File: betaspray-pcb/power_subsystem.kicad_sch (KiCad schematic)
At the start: 1 part, among them U2 LM3940IT-3.3

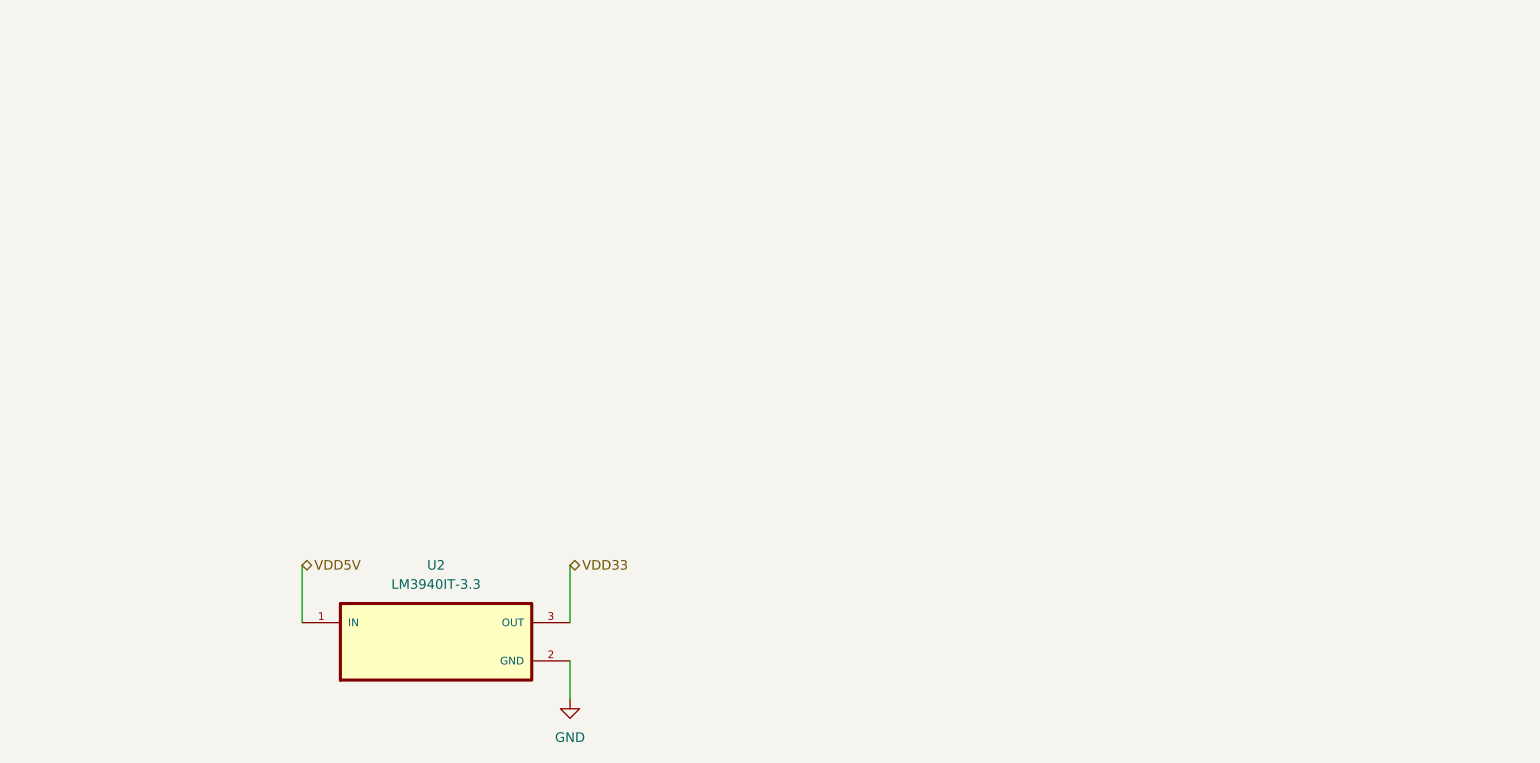
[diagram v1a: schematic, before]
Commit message: Add USB-C, connection, power decoupling
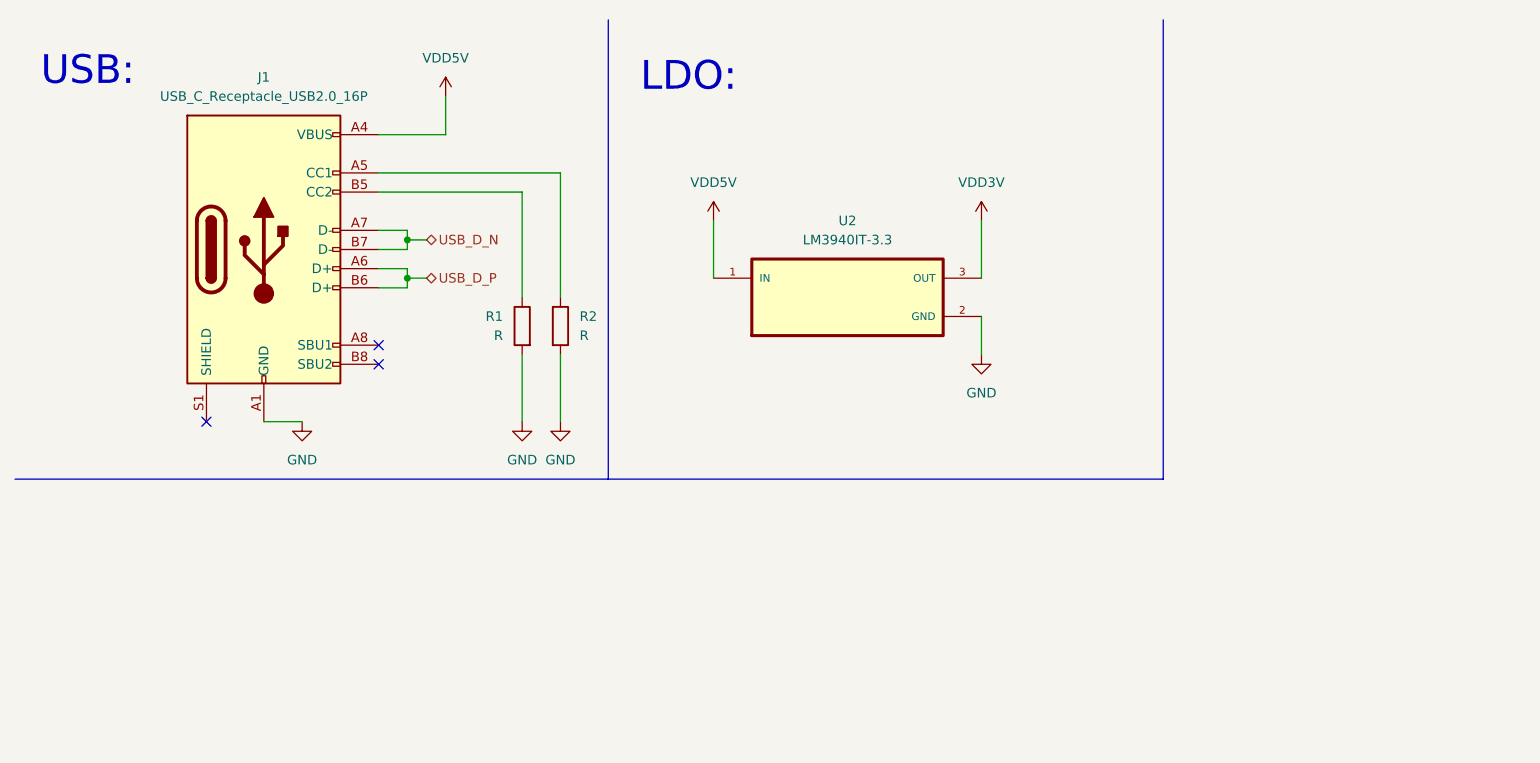
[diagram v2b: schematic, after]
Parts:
- added J1: USB_C_Receptacle_USB2.0_16P, Connector_USB:USB_C_Receptacle_G-Switch_GT-USB-7010ASV, symbol betaspray_Connector:USB_C_Receptacle_USB2.0_16P
- added R1, R2: R, symbol betaspray_LDO:R
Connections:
- net GND: now also J1.A1 (GND), J1.A12 (GND), J1.B1 (GND), J1.B12 (GND), R1.2, R2.2
- net VDD5V: now also J1.A4 (VBUS), J1.A9 (VBUS), J1.B4 (VBUS), J1.B9 (VBUS)
- net VDD33 renamed VDD3V
- new net: J1.B5 (CC2), R1.1
- new net: J1.A5 (CC1), R2.1
- new net USB_D_N: J1.A7 (D-), J1.B7 (D-)
- new net USB_D_P: J1.A6 (D+), J1.B6 (D+)
- no-connect marks 0 -> 3
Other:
- note added: "LDO:"
- note added: "USB:"
- moved on the sheet: U2

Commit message: status led ???
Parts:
- added C4: 0.47 uF, symbol betaspray_LDO:C
- added C5: 33 uF, symbol Device:C
- added D1: LED, LED_SMD:LED_0805_2012Metric, symbol betaspray_LDO:LED
- added R3: 300, symbol betaspray_LDO:R
- R1, R2: value R -> 5.1k
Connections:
- net GND: now also C4.2, C5.2, R3.2
- net VDD3V: now also C5.1, D1.2 (A)
- net VDD5V: now also C4.1
- new net: D1.1 (K), R3.1
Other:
- note added: "These are the recommended input/output capacitance, per TI's datasheet."
- note added: "am i stupid"

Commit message: Connected Servo labels, added debug led
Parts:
- C4: symbol betaspray_LDO:C -> betaspray_MCU_Espressif:C
- C5: symbol Device:C -> betaspray_MCU_Espressif:C
- D1: symbol betaspray_LDO:LED -> betaspray_MCU_Espressif:LED
- J1: symbol betaspray_Connector:USB_C_Receptacle_USB2.0_16P -> betaspray_MCU_Espressif:USB_C_Receptacle_USB2.0_16P
- R1, R2, R3: symbol betaspray_LDO:R -> betaspray_MCU_Espressif:R
- U2: symbol betaspray_Connector:LM3940IT-3.3 -> betaspray_MCU_Espressif:LM3940IT-3.3
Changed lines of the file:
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@@
 	)
 	(symbol
-		(lib_id "betaspray_Connector:GND")
+		(lib_id "betaspray_MCU_Espressif:GND")
 		(at 78.74 64.77 0)
 		(unit 1)
@@
 	)
 	(symbol
-		(lib_id "betaspray_Connector:LM3940IT-3.3")
+		(lib_id "betaspray_MCU_Espressif:LM3940IT-3.3")
 		(at 121.92 48.26 0)
 		(unit 1)
@@
 	)
 	(symbol
-		(lib_id "betaspray_LDO:C")
+		(lib_id "betaspray_MCU_Espressif:C")
 		(at 104.14 54.61 0)
 		(mirror y)
@@
 	)
 	(symbol
-		(lib_id "betaspray_Connector:+3.3V")
+		(lib_id "betaspray_MCU_Espressif:+3.3V")
 		(at 139.7 38.1 0)
 		(unit 1)
@@
 	)
 	(symbol
-		(lib_id "betaspray_Connector:GND")
+		(lib_id "betaspray_MCU_Espressif:GND")
 		(at 139.7 64.77 0)
 		(unit 1)
@@
 	)
 	(symbol
-		(lib_id "betaspray_LDO:R")
+		(lib_id "betaspray_MCU_Espressif:R")
 		(at 78.74 52.07 0)
 		(mirror y)
@@
 	)
 	(symbol
-		(lib_id "Device:C")
+		(lib_id "betaspray_MCU_Espressif:C")
 		(at 147.32 54.61 0)
 		(unit 1)
@@
 	)
 	(symbol
-		(lib_id "betaspray_Connector:GND")
+		(lib_id "betaspray_MCU_Espressif:GND")
 		(at 83.82 64.77 0)
 		(unit 1)
@@
 	)
 	(symbol
-		(lib_id "betaspray_Connector:+3.3V")
+		(lib_id "betaspray_MCU_Espressif:+3.3V")
 		(at 182.88 21.59 0)
 		(unit 1)
@@
 	)
 	(symbol
-		(lib_id "betaspray_LDO:LED")
+		(lib_id "betaspray_MCU_Espressif:LED")
 		(at 182.88 31.75 90)
 		(unit 1)
@@
 	)
 	(symbol
-		(lib_id "betaspray_Connector:GND")
+		(lib_id "betaspray_MCU_Espressif:GND")
 		(at 49.53 64.77 0)
 		(unit 1)
@@
 	)
 	(symbol
-		(lib_id "power:+5V")
+		(lib_id "betaspray_MCU_Espressif:+5V")
 		(at 104.14 38.1 0)
 		(unit 1)
@@
 	)
 	(symbol
-		(lib_id "betaspray_Connector:USB_C_Receptacle_USB2.0_16P")
+		(lib_id "betaspray_MCU_Espressif:USB_C_Receptacle_USB2.0_16P")
 		(at 44.45 41.91 0)
 		(unit 1)
@@
 	)
 	(symbol
-		(lib_id "betaspray_LDO:R")
+		(lib_id "betaspray_MCU_Espressif:R")
 		(at 83.82 52.07 0)
 		(unit 1)
@@
 	)
 	(symbol
-		(lib_id "betaspray_Connector:GND")
+		(lib_id "betaspray_MCU_Espressif:GND")
 		(at 182.88 58.42 0)
 		(unit 1)
@@
 	)
 	(symbol
-		(lib_id "betaspray_LDO:R")
+		(lib_id "betaspray_MCU_Espressif:R")
 		(at 182.88 46.99 0)
 		(unit 1)
@@
 	)
 	(symbol
-		(lib_id "power:+5V")
+		(lib_id "betaspray_MCU_Espressif:+5V")
 		(at 68.58 21.59 0)
 		(unit 1)

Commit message: Started layout
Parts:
- C4, C5: footprint (none) -> Capacitor_SMD:C_0805_2012Metric_Pad1.18x1.45mm_HandSolder
- R1, R2, R3: footprint (none) -> Resistor_SMD:R_0805_2012Metric_Pad1.20x1.40mm_HandSolder
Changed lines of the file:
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@@
 			)
 		)
-		(property "Footprint" ""
+		(property "Footprint" "Capacitor_SMD:C_0805_2012Metric_Pad1.18x1.45mm_HandSolder"
 			(at 103.1748 58.42 0)
 			(effects
@@
 			)
 		)
-		(property "Footprint" ""
+		(property "Footprint" "Resistor_SMD:R_0805_2012Metric_Pad1.20x1.40mm_HandSolder"
 			(at 80.518 52.07 90)
 			(effects
@@
 			)
 		)
-		(property "Footprint" ""
+		(property "Footprint" "Capacitor_SMD:C_0805_2012Metric_Pad1.18x1.45mm_HandSolder"
 			(at 148.2852 58.42 0)
 			(effects
@@
 			)
 		)
-		(property "Footprint" ""
+		(property "Footprint" "Resistor_SMD:R_0805_2012Metric_Pad1.20x1.40mm_HandSolder"
 			(at 82.042 52.07 90)
 			(effects
@@
 			)
 		)
-		(property "Footprint" ""
+		(property "Footprint" "Resistor_SMD:R_0805_2012Metric_Pad1.20x1.40mm_HandSolder"
 			(at 181.102 46.99 90)
 			(effects

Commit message: Trying to route
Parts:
- U2: footprint LM3940IT-3.3:TO254P1054X470X1955-3 -> LDO:TO254P1054X470X1955-3
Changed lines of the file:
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@@
 			)
 		)
-		(property "Footprint" "LM3940IT-3.3:TO254P1054X470X1955-3"
+		(property "Footprint" "LDO:TO254P1054X470X1955-3"
 			(at 121.92 48.26 0)
 			(effects

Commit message: Trying to route
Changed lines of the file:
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@@
+		)
+	)
+	(hierarchical_label "VDD3V"
+		(shape input)
+		(at 139.7 38.1 0)
+		(effects
+			(font
+				(size 1.27 1.27)
+			)
+			(justify left)
 		)
 	)
@@
 					(unit 1)
 				)
-			)
-		)
-	)
-	(symbol
-		(lib_id "betaspray_MCU_Espressif:+3.3V")
-		(at 139.7 38.1 0)
-		(unit 1)
-		(exclude_from_sim no)
-		(in_bom yes)
-		(on_board yes)
-		(dnp no)
-		(fields_autoplaced yes)
-		(property "Reference" "#PWR03"
-			(at 139.7 41.91 0)
-			(effects
-				(font
-					(size 1.27 1.27)
-				)
-				(hide yes)
-			)
-		)
-		(property "Value" "VDD3V"
-			(at 139.7 33.02 0)
-			(effects
-				(font
-					(size 1.27 1.27)
-				)
-			)
-		)
-		(property "Footprint" ""
-			(at 139.7 38.1 0)
-			(effects
-				(font
-					(size 1.27 1.27)
-				)
-				(hide yes)
-			)
-		)
-		(property "Datasheet" ""
-			(at 139.7 38.1 0)
-			(effects
-				(font
-					(size 1.27 1.27)
-				)
-				(hide yes)
-			)
-		)
-		(property "Description" "Power symbol creates a global label with name \"+3.3V\""
-			(at 139.7 38.1 0)
-			(effects
-				(font
-					(size 1.27 1.27)
-				)
-				(hide yes)
-			)
-		)
-		(pin "1"
-		)
-		(instances
-			(project ""
-				(path "/5d34c70f-469d-43be-b671-484e3b695429/48241481-8c99-4c08-b4b7-9ff4b52e25cf"
-					(reference "#PWR03")
-					(unit 1)
-				)
